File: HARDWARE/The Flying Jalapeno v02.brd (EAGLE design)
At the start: 73.7 x 72.4 mm, 97 parts, among them Q2 MMBT2222A, Q3 NDP6020P, Q4 MMBT2222A, Q5 NDP6020P, Q6 BSS138, 200mA/50V, Q7 BSS138, 200mA/50V, U1 ATMEGA2560AU, U2 LM1117, U3 LM1117, U4 LM1117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

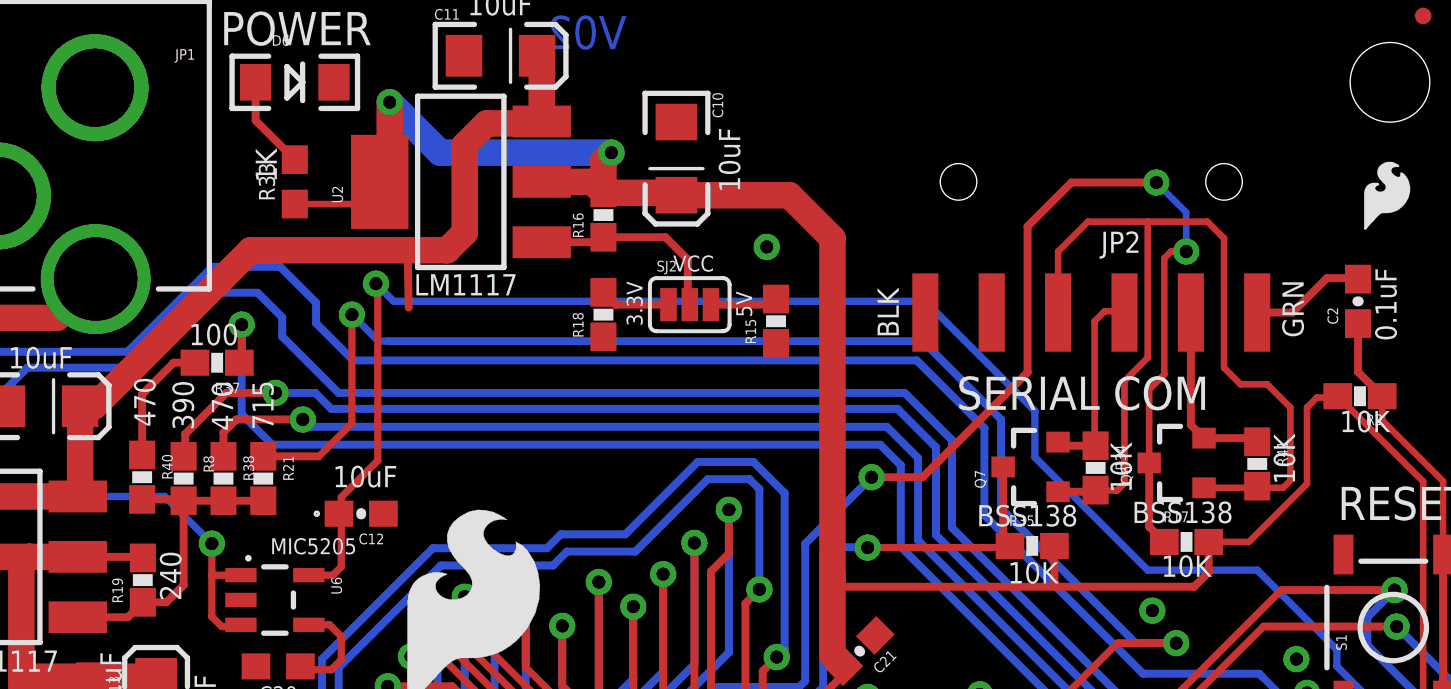
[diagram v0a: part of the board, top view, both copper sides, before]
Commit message: corrected Resistor names
Some resistor names skipped  in the 30s, now they increment correctly.
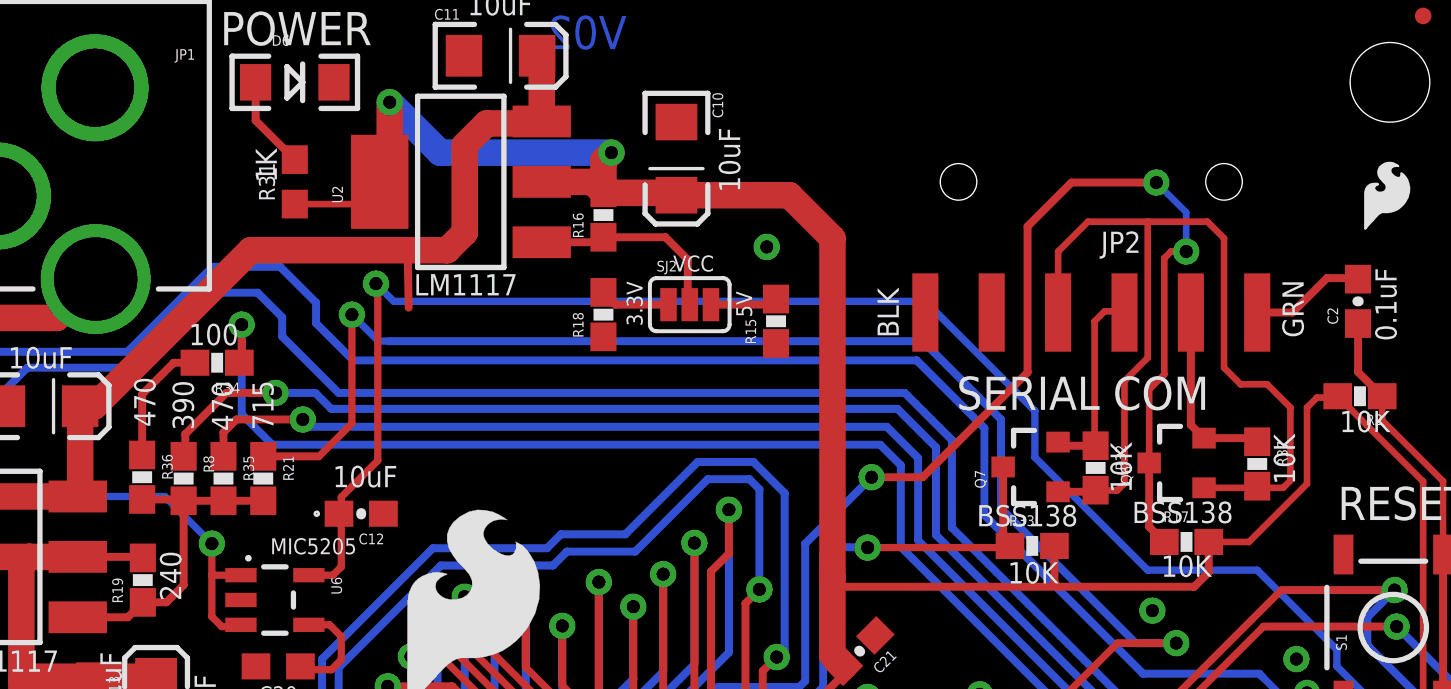
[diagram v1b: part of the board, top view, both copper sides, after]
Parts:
- removed R38: 470, SparkFun-Resistors:0603-RES
- removed R41: 10K, SparkFun-Resistors:0603-RES
- added R31: 1k, SparkFun-Resistors:0603
- added R32: 10K, SparkFun-Resistors:0603-RES
- R33: value 1k -> 10K; device SparkFun-Resistors:0603 -> SparkFun-Resistors:0603-RES
- R34: value 10K -> 100
- R35: value 10K -> 470
- R37: value 100 -> 10K
- moved R37 40.0 mm to (64.8, 54.0), turned to 270 degrees
- moved R34 33.9 mm to (25.0, 57.8), turned to 180 degrees
- moved R33 31.5 mm to (56.2, 50.8), turned to 0 degrees
- moved R35 31.1 mm to (25.2, 53.4), turned to 270 degrees
- renumbered R40 to R36
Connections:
- net 37/V2_3.7V: now also R35.1; no longer R38.1
- net 38/V2_4.2V: now also R34.1; no longer R37.1
- net FTDI_VCC: now also R32.2, R37.2; no longer R34.2, R41.2
- net N$1: now also R34.2; no longer R37.2
- net N$10: now also R35.2; no longer R38.2
- net N$16: now also R32.1; no longer R34.1
- net N$25: now also R31.2; no longer R33.2
- net N$26: now also R37.1; no longer R41.1
- net RX0: now also R33.1; no longer R35.1
- net VCC: now also R31.1, R33.2; no longer R33.1, R35.2
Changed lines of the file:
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@@
 <?xml version="1.0" encoding="utf-8"?>
 <!DOCTYPE eagle SYSTEM "eagle.dtd">
-<eagle version="7.5.0">
+<eagle version="7.6.0">
 <drawing>
 <settings>
@@
 <element name="STANDOFF3" library="SparkFun-Electromechanical" package="STAND-OFF-TIGHT" value="STAND-OFFTIGHT" x="69.85" y="68.58"/>
 <element name="STANDOFF4" library="SparkFun-Electromechanical" package="STAND-OFF-TIGHT" value="STAND-OFFTIGHT" x="3.81" y="68.58"/>
-<element name="R37" library="SparkFun-Resistors" package="0603-RES" value="100" x="24.9682" y="57.8485" rot="R180">
+<element name="R34" library="SparkFun-Resistors" package="0603-RES" value="100" x="24.9682" y="57.8485" rot="R180">
 <attribute name="PROD_ID" value="RES-07863" x="24.9682" y="57.8485" size="1.778" layer="27" font="vector" ratio="15" rot="R180" display="off"/>
 </element>
-<element name="R38" library="SparkFun-Resistors" package="0603-RES" value="470" x="25.2095" y="53.4162" rot="R270">
+<element name="R35" library="SparkFun-Resistors" package="0603-RES" value="470" x="25.2095" y="53.4162" rot="R270">
 <attribute name="PROD_ID" value="RES-07869" x="25.2095" y="53.4162" size="1.778" layer="27" font="vector" ratio="15" rot="R270" display="off"/>
 </element>
@@
 <attribute name="PROD_ID" value="DIO-00809" x="27.94" y="68.58" size="1.778" layer="27" font="vector" ratio="15" display="off"/>
 </element>
-<element name="R33" library="SparkFun-Resistors" package="0603" value="1k" x="27.94" y="64.77" rot="R90">
+<element name="R31" library="SparkFun-Resistors" package="0603" value="1k" x="27.94" y="64.77" rot="R90">
 <attribute name="PROD_ID" value="RES-07856" x="27.94" y="64.77" size="1.778" layer="27" font="vector" ratio="15" rot="R90" display="off"/>
 </element>
@@
 <attribute name="VALUE" value="200mA/50V" x="56.1467" y="53.8607" size="1.778" layer="27" rot="R90" display="off"/>
 </element>
-<element name="R41" library="SparkFun-Resistors" package="0603-RES" value="10K" x="64.77" y="53.975" rot="R270">
+<element name="R37" library="SparkFun-Resistors" package="0603-RES" value="10K" x="64.77" y="53.975" rot="R270">
 <attribute name="PROD_ID" value="RES-00824" x="64.77" y="53.975" size="1.778" layer="27" font="vector" ratio="15" rot="R270" display="off"/>
 </element>
@@
 <attribute name="PROD_ID" value="RES-00824" x="62.0649" y="50.9905" size="1.778" layer="27" font="vector" ratio="15" display="off"/>
 </element>
-<element name="R34" library="SparkFun-Resistors" package="0603-RES" value="10K" x="58.5851" y="53.8226" rot="R270">
+<element name="R32" library="SparkFun-Resistors" package="0603-RES" value="10K" x="58.5851" y="53.8226" rot="R270">
 <attribute name="PROD_ID" value="RES-00824" x="58.5851" y="53.8226" size="1.778" layer="27" font="vector" ratio="15" rot="R270" display="off"/>
 </element>
-<element name="R35" library="SparkFun-Resistors" package="0603-RES" value="10K" x="56.1594" y="50.8381">
+<element name="R33" library="SparkFun-Resistors" package="0603-RES" value="10K" x="56.1594" y="50.8381">
 <attribute name="PROD_ID" value="RES-00824" x="56.1594" y="50.8381" size="1.778" layer="27" font="vector" ratio="15" display="off"/>
 </element>
-<element name="R40" library="SparkFun-Resistors" package="0603-RES" value="470" x="22.098" y="53.467" rot="R270">
+<element name="R36" library="SparkFun-Resistors" package="0603-RES" value="470" x="22.098" y="53.467" rot="R270">
 <attribute name="PROD_ID" value="RES-07869" x="22.098" y="53.467" size="1.778" layer="27" font="vector" ratio="15" rot="R270" display="off"/>
 </element>
@@
 <contactref element="C22" pad="2"/>
 <contactref element="R17" pad="2"/>
-<contactref element="R35" pad="2"/>
+<contactref element="R33" pad="2"/>
 <wire x1="39.751" y1="64.35" x2="42.454" y2="64.35" width="1.016" layer="1"/>
 <wire x1="42.454" y1="64.35" x2="42.545" y2="64.259" width="1.016" layer="1"/>
@@
 <wire x1="63.2714" y1="27.9654" x2="63.2714" y2="25.923240625" width="0.254" layer="1"/>
 <wire x1="63.2714" y1="25.923240625" x2="64.137540625" y2="25.0571" width="0.254" layer="1"/>
-<contactref element="R33" pad="1"/>
+<contactref element="R31" pad="1"/>
 <wire x1="31.191" y1="64.77" x2="30.341" y2="63.92" width="0.254" layer="1"/>
 <wire x1="30.341" y1="63.92" x2="27.94" y2="63.92" width="0.254" layer="1"/>
@@
 <contactref element="R21" pad="2"/>
 <contactref element="R8" pad="2"/>
-<contactref element="R38" pad="2"/>
+<contactref element="R35" pad="2"/>
 <wire x1="19.6342" y1="48.1076" x2="21.551" y2="48.1076" width="0.3048" layer="1"/>
 <wire x1="21.551" y1="48.1076" x2="22.1234" y2="48.68" width="0.3048" layer="1"/>
@@
 <wire x1="25.146" y1="52.5027" x2="25.2095" y2="52.5662" width="0.3048" layer="1"/>
 <wire x1="25.2095" y1="52.5662" x2="26.7335" y2="52.5662" width="0.3048" layer="1"/>
-<contactref element="R40" pad="2"/>
+<contactref element="R36" pad="2"/>
 <wire x1="23.026" y1="48.68" x2="23.6855" y2="49.3395" width="0.3048" layer="1"/>
 <wire x1="23.6855" y1="49.3395" x2="23.6855" y2="52.5662" width="0.3048" layer="1"/>
@@
 <contactref element="U1" pad="2"/>
 <contactref element="Q7" pad="3"/>
-<contactref element="R35" pad="1"/>
+<contactref element="R33" pad="1"/>
 <wire x1="55.0467" y1="53.8607" x2="55.0467" y2="51.1008" width="0.3048" layer="1"/>
 <wire x1="55.0467" y1="51.1008" x2="55.3094" y2="50.8381" width="0.3048" layer="1"/>
@@
 <signal name="38/V2_4.2V">
 <contactref element="U1" pad="50"/>
-<contactref element="R37" pad="1"/>
+<contactref element="R34" pad="1"/>
 <via x="65.405" y="33.4518" extent="1-16" drill="0.508"/>
 <wire x1="51.1302" y1="50.8" x2="51.1302" y2="53.9242" width="0.3048" layer="16"/>
@@
 <signal name="37/V2_3.7V">
 <contactref element="U1" pad="53"/>
-<contactref element="R38" pad="1"/>
+<contactref element="R35" pad="1"/>
 <wire x1="60.364359375" y1="36.03934375" x2="61.409015625" y2="37.084" width="0.2794" layer="1"/>
 <wire x1="61.409015625" y1="37.084" x2="63.4238" y2="37.084" width="0.3048" layer="1"/>
@@
 <signal name="N$25">
 <contactref element="D6" pad="A"/>
-<contactref element="R33" pad="2"/>
+<contactref element="R31" pad="2"/>
 <wire x1="27.94" y1="65.62" x2="26.44" y2="67.12" width="0.3048" layer="1"/>
 <wire x1="26.44" y1="67.12" x2="26.44" y2="68.58" width="0.3048" layer="1"/>
@@
 <contactref element="Q6" pad="1"/>
 <contactref element="Q7" pad="1"/>
-<contactref element="R41" pad="2"/>
-<contactref element="R34" pad="2"/>
+<contactref element="R37" pad="2"/>
+<contactref element="R32" pad="2"/>
 <contactref element="JP2" pad="4"/>
 <wire x1="57.1467" y1="52.9107" x2="58.9042" y2="52.9107" width="0.3048" layer="1"/>
@@
 <signal name="N$16">
 <contactref element="Q7" pad="2"/>
-<contactref element="R34" pad="1"/>
+<contactref element="R32" pad="1"/>
 <wire x1="58.5851" y1="54.6726" x2="57.2848" y2="54.6726" width="0.3048" layer="1"/>
 <wire x1="57.2848" y1="54.6726" x2="57.1467" y2="54.8107" width="0.3048" layer="1"/>
@@
 <signal name="N$26">
 <contactref element="Q6" pad="2"/>
-<contactref element="R41" pad="1"/>
+<contactref element="R37" pad="1"/>
 <wire x1="62.23" y1="55.4678" x2="62.7347" y2="54.9631" width="0.3048" layer="1"/>
 <wire x1="62.7347" y1="54.9631" x2="64.6319" y2="54.9631" width="0.3048" layer="1"/>
@@
 </signal>
 <signal name="N$1">
-<contactref element="R40" pad="1"/>
-<contactref element="R37" pad="2"/>
+<contactref element="R36" pad="1"/>
+<contactref element="R34" pad="2"/>
 <wire x1="22.098" y1="54.317" x2="22.098" y2="56.642" width="0.3048" layer="1"/>
 <wire x1="22.098" y1="56.642" x2="23.3045" y2="57.8485" width="0.3048" layer="1"/>
